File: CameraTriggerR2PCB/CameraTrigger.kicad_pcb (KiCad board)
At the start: 2 copper layers, 95.2 x 90.2 mm, 57 parts, among them J1 Power, J10 feather short, J11 Ada2633, J12 Camera 2.5mm, J13 +5V Always on, J14 Ext power switch, J2 Camera 3.5mm, J3 Aux out, J4 HighLowIn, J5 Laser, J6 Sensor, J7 Trig, J8 Arm, J9 Ada3178, Q1 PN2222A, Q2 PN2222A, Q3 PN2222A, SW1 SW_Power, SW2 SW_Trigger, SW3 SW_Poll, SW4 SW_Arm, U1 LM7805_TO220, U2 ILD74, U3 ILD74

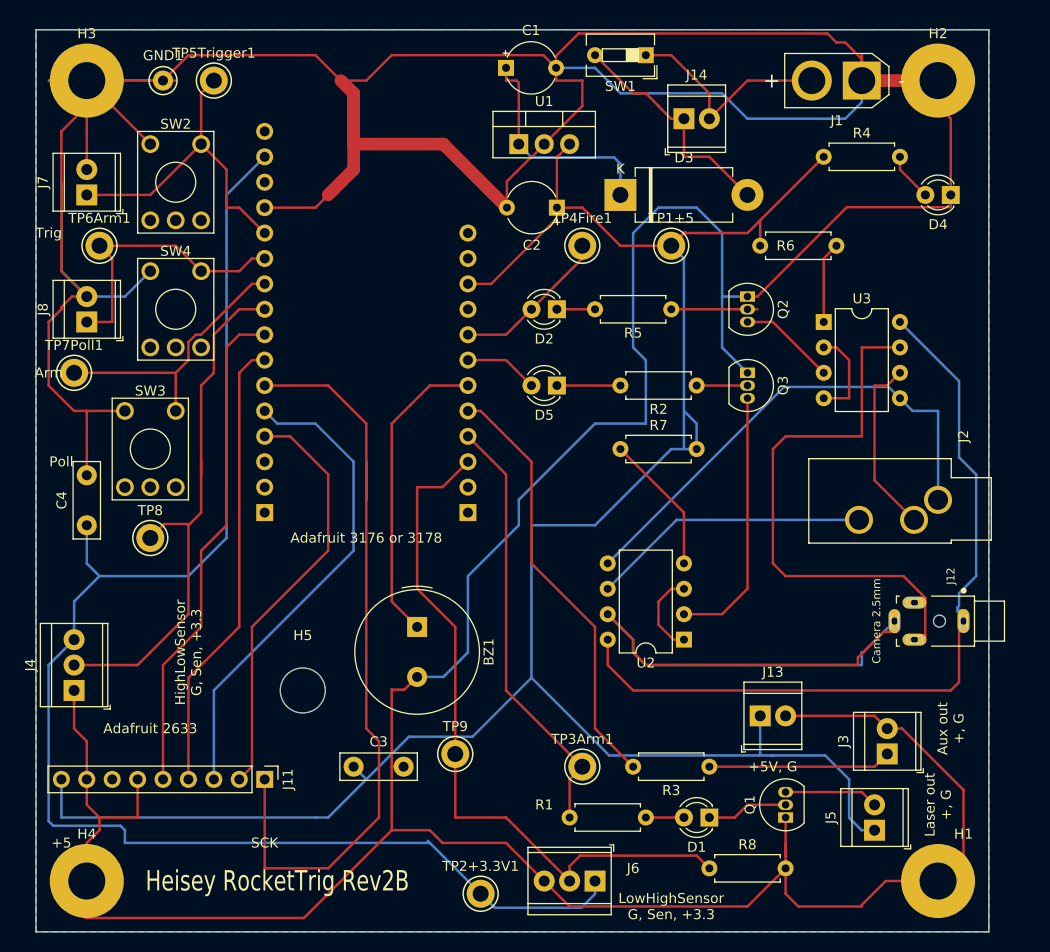
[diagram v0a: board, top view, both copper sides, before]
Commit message: Moved jacks closer to board edge
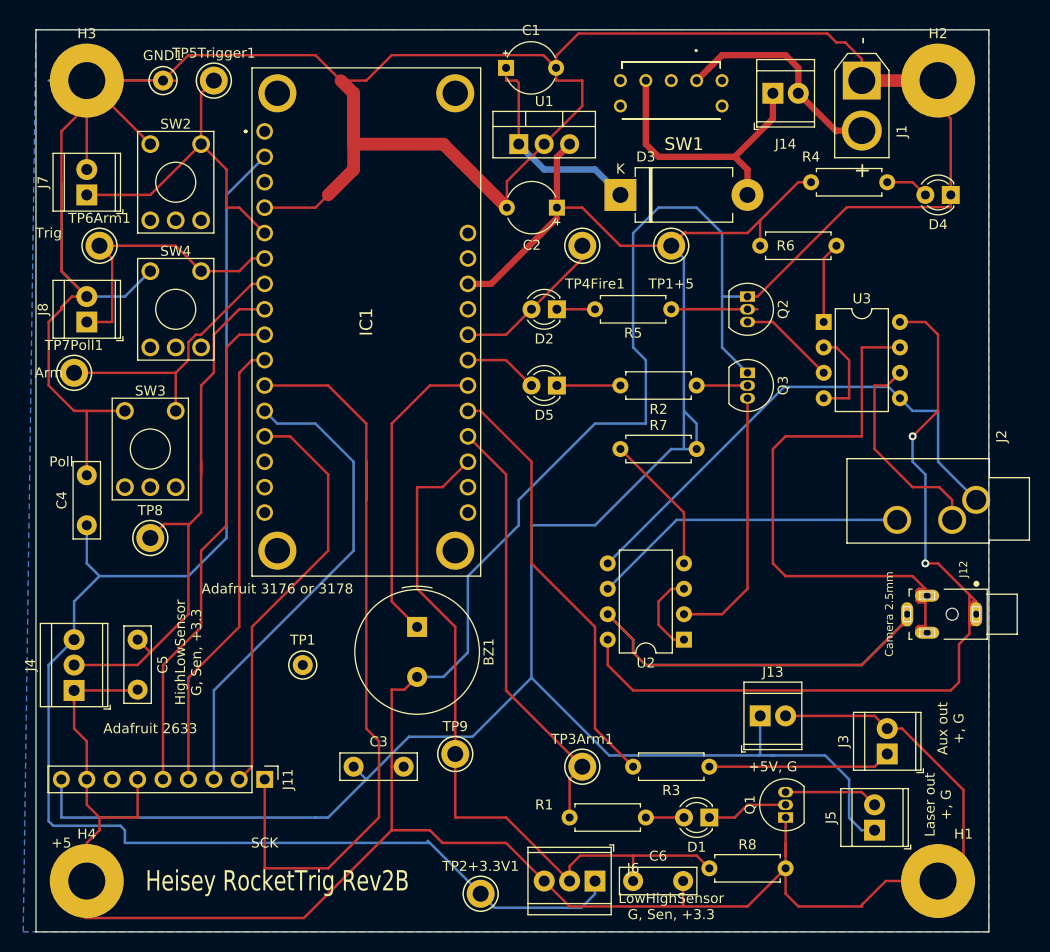
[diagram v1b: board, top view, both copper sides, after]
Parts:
- removed H5: MountingHole, MountingHole:MountingHole_4.5mm
- removed J10: feather short, Connector_PinHeader_2.54mm:PinHeader_1x12_P2.54mm_Vertical
- removed J9: Ada3178, Connector_PinHeader_2.54mm:PinHeader_1x16_P2.54mm_Vertical
- added C5: 0.01 μF, Capacitor_THT:C_Disc_D7.5mm_W2.5mm_P5.00mm, F.Cu at (26.7, 73.7)
- added C6: 0.01 μF, Capacitor_THT:C_Disc_D7.5mm_W2.5mm_P5.00mm, F.Cu at (76.2, 97.8)
- added IC1: 3178, 3178, F.Cu at (39.4, 22.9)
- added TP1: TestPoint, TestPoint:TestPoint_Keystone_5000-5004_Miniature, F.Cu at (43.2, 76.2)
- SW1: value SW_Power -> AS11CB; footprint Button_Switch_THT:SW_DIP_SPSTx01_Slide_6.7x4.1mm_W7.62mm_P2.54mm_LowProfile -> CameraTriggerPCB:AS11CB
- moved J14 9.25 mm to (90.2, 19.1)
- moved SW1 4.58 mm to (82.5, 17.8), turned to 270 degrees
- moved J2 3.81 mm to (110.5, 59.7)
- moved R4 2.84 mm to (94.0, 27.9)
- moved J12 1.45 mm to (110.5, 71.1)
- turned J1 to 270 degrees
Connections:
- SW1 pad 2: Net-(D3-Pad2) -> Net-(SW1-Pad2)
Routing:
- net GND: track 623.2 -> 594.0 mm
- net Net-(J12-PadS): track 77.8 -> 87.2 mm, vias 0 -> 2
- net Net-(D3-Pad2): track 23.3 -> 28.0 mm
- net Net-(J2-PadR): track 28.0 -> 31.8 mm
- net Net-(J2-PadT): track 18.1 -> 21.3 mm
- net Net-(J12-PadR): track 66.6 -> 69.4 mm
- net SensorIn: track 71.2 -> 73.7 mm
- net +5V: track 221.6 -> 219.3 mm
- net AuxIn: track 54.4 -> 56.2 mm
- net Net-(J12-PadT): track 55.1 -> 56.8 mm
- net Net-(J2-PadS): track 50.2 -> 51.8 mm
- net Net-(C1-Pad1): track 21.6 -> 21.1 mm
- net Net-(D4-Pad2): track 4.86 -> 4.34 mm
